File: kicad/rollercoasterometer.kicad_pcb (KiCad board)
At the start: 2 copper layers, 66 x 94 mm, 133 parts, among them J101 USB_C_Receptacle, J120 STANDOFF, J125 STANDOFF, J127 STANDOFF, J129 STANDOFF, J1401 USB_C_Receptacle, J1402 USB_C_Receptacle, J1601 USB_C_Receptacle, J1602 USB_C_Receptacle, J3501 Conn_01x10, J3502 Conn_01x10, J401 SMA, J402 SolderJumper_2_Open, Q2001 NMOS, Q3101 NMOS, Q801 NMOS, U1001 TCR2EF 1.8V, U104 Teensy4.1, U1101 BMM150, U1201 ICM-42688, U1301 ICM-42688, U1801 TLE493D-W2B6, U1901 TCR2EF 1.8V, U201 ICM-42688, U2101 ICM-42688, U2201 BMM150, U2401 AK09918, U2501 BMP384, U2701 ICM-42688, U2801 TLE493D-W2B6, U2901 BMP384, U3001 TCR2EF 1.8V, U301 USBLC6-4SC6, U3201 ICM-42688, U3301 BMM150, U3401 AK09918, U401 ZED_F9R, U501 TCR2EF 3.3V, U601 AK09918, U704 TLE493D-W2B6, U901 BMP384

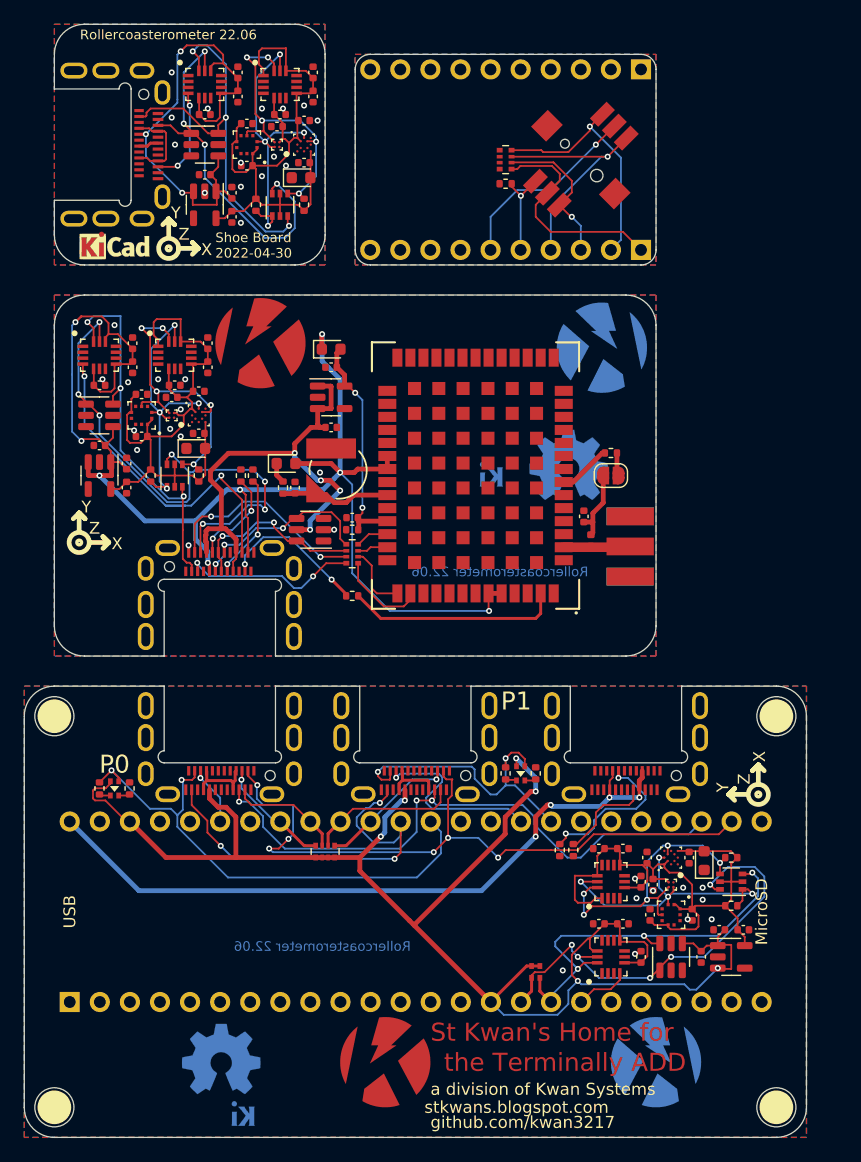
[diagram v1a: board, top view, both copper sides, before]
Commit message: Moved USB+ connectors to bottom of board
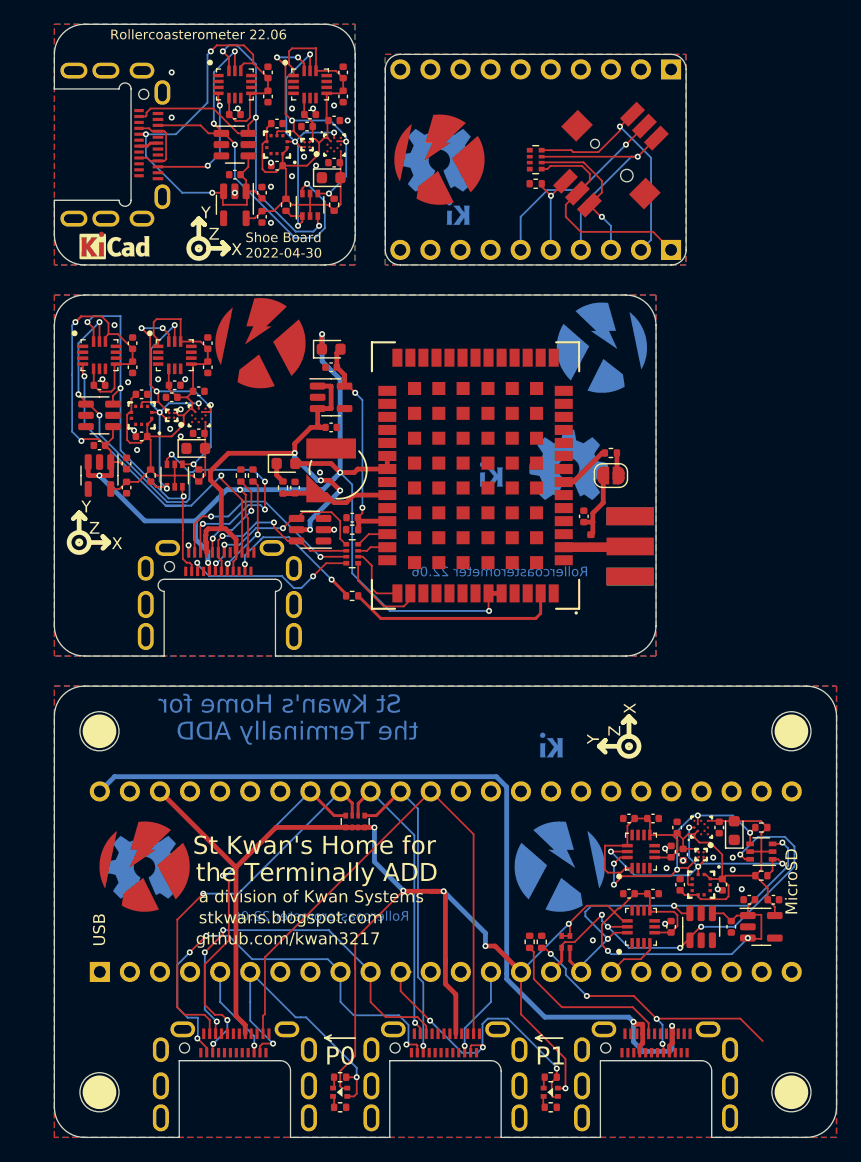
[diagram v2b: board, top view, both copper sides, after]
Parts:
- added G3502: KwanSystems, KwanSystems:StKwansSoldermask, F.Cu at (108.7, 72.4)
- added G3503: DesignedWithKicad, KwanSystems:Symbol_KiCAD-Logo_CopperAndSilkScreenTop_small, B.Cu at (108.5, 77.0)
- added G3504: OSHW, KwanSystems:OSHW-Symbol_6.7x6mm_SolderMask, B.Cu at (108.7, 72.1)
- G101: moved to F.Cu
- G102: moved to B.Cu
- moved G101 46.2 mm to (83.8, 132.1), turned to 0 degrees
- moved G103 40.6 mm to (116.3, 121.9)
- moved J101 38.2 mm to (127.0, 154.9), turned to 0 degrees
- moved J1601 38.2 mm to (109.2, 154.9), turned to 0 degrees
- moved J1401 38.1 mm to (91.4, 154.9), turned to 0 degrees
- moved R1401 32.3 mm to (100.3, 152.4), turned to 0 degrees
- moved D1401 32.0 mm to (100.3, 151.1), turned to 0 degrees
- moved R1402 31.7 mm to (100.3, 149.9), turned to 0 degrees
- moved R1601 28.2 mm to (118.1, 152.4), turned to 0 degrees
- moved D1601 27.0 mm to (118.1, 151.1), turned to 0 degrees
- moved R1602 25.9 mm to (118.1, 149.9), turned to 0 degrees
- moved G102 22.1 mm to (118.9, 132.1), turned to 180 degrees
- moved G104 17.7 mm to (83.8, 131.8)
- moved G105 11.7 mm to (124.7, 121.9)
- moved R101 8.58 mm to (116.3, 138.4), turned to -90 degrees
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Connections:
- U104 pad 10: unconnected-(U104-Pad10) -> /RX_GPS
- U104 pad 11: unconnected-(U104-Pad11) -> /P1_ID
- U104 pad 14: unconnected-(U104-Pad14) -> /P1_INT
- U104 pad 26: /TX_GPS -> unconnected-(U104-Pad26)
- U104 pad 27: /RX_GPS -> unconnected-(U104-Pad27)
- U104 pad 32: /P1_ID -> unconnected-(U104-Pad32)
- U104 pad 33: /P1_INT -> unconnected-(U104-Pad33)
- U104 pad 36: /P0_ID -> unconnected-(U104-Pad36)
- U104 pad 43: /P0_INT -> unconnected-(U104-Pad43)
- U104 pad 5: unconnected-(U104-Pad5) -> /P0_INT
- U104 pad 6: unconnected-(U104-Pad6) -> /P0_ID
- U104 pad 9: unconnected-(U104-Pad9) -> /TX_GPS
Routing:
- net /P0_SDA: track 9.50 -> 32.5 mm, vias 0 -> 1
- net /P0_SCL: track 9.80 -> 31.9 mm, vias 1 -> 3
- net /TX_GPS: track 59.0 -> 37.4 mm, vias 6 -> 4
- net +3V3: track 131.7 -> 152.8 mm, vias 6 -> 8
- net /P0_ID: track 43.6 -> 24.9 mm
- net /RX_GPS: track 50.1 -> 32.5 mm
- net +5V: track 59.6 -> 76.7 mm, vias 4 -> 2
- net /P1_SCL: track 11.7 -> 26.7 mm
- net /PPS: track 34.5 -> 48.3 mm, vias 3 -> 0
- net /CC2: track 13.3 -> 25.4 mm, vias 2 -> 4
- net /P1_SDA: track 12.7 -> 24.7 mm, vias 0 -> 1
- net /P1_INT: track 16.1 -> 7.74 mm
- net /CC1: track 8.11 -> 14.9 mm
- net unconnected-(J1401-PadA4): track 5.72 -> 0.00 mm
- net /Shoe/Q_3V3: track 41.7 -> 46.8 mm
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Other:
- outline, holes or cut-outs redrawn
- board text added: "Interface Board 2022-04-30"
- board text added: "St Kwan's Home for"
- board text added: "the Terminally ADD"

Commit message: Added a NC to the board
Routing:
- net /CC2: track 25.4 -> 15.6 mm
- net +3V3: track 152.8 -> 150.2 mm, vias 8 -> 7
- net /P1_ID: track 26.8 -> 25.9 mm
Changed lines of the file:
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@@
       (net 82 "/TV_D{slash}~{C}") (pinfunction "D5~") (pintype "bidirectional"))
     (pad "8" thru_hole oval locked (at 0 17.78 90) (size 1.7 1.7) (drill 1) (layers *.Cu *.Mask)
-      (net 239 "unconnected-(U104-Pad8)") (pinfunction "D6~") (pintype "bidirectional"))
+      (net 239 "unconnected-(U104-Pad8)") (pinfunction "D6~") (pintype "bidirectional+no_connect"))
     (pad "9" thru_hole oval locked (at 0 20.32 90) (size 1.7 1.7) (drill 1) (layers *.Cu *.Mask)
       (net 75 "/TX_GPS") (pinfunction "D7~") (pintype "bidirectional"))
@@
   (segment (start 99.3679 137.4399) (end 90.4499 137.4399) (width 0.1524) (layer "B.Cu") (net 72))
   (segment (start 134.7525 135.4755) (end 134.7525 136.21) (width 0.1524) (layer "F.Cu") (net 73))
+  (segment (start 110.095 142.861) (end 109.22 141.986) (width 0.4064) (layer "F.Cu") (net 73))
   (segment (start 101.6 140.716) (end 101.6 148.082) (width 0.1524) (layer "F.Cu") (net 73))
   (segment (start 125.194 134.366) (end 123.952 135.608) (width 0.1524) (layer "F.Cu") (net 73))
@@
   (segment (start 124.214 136.66) (end 123.444 135.89) (width 0.1524) (layer "F.Cu") (net 73))
   (segment (start 121.158 135.382) (end 119.634 136.906) (width 0.1524) (layer "F.Cu") (net 73))
-  (segment (start 109.22 134.3152) (end 109.0676 134.1628) (width 0.4064) (layer "F.Cu") (net 73))
   (segment (start 135.065742 138.176) (end 135.89 138.176) (width 0.1524) (layer "F.Cu") (net 73))
+  (segment (start 110.095 146.19) (end 110.095 142.861) (width 0.4064) (layer "F.Cu") (net 73))
   (segment (start 113.4136 138.7856) (end 115.598 140.97) (width 0.4064) (layer "F.Cu") (net 73))
   (segment (start 123.444 135.89) (end 122.936 135.382) (width 0.1524) (layer "F.Cu") (net 73))
@@
   (segment (start 123.952 135.608) (end 123.797 135.608) (width 0.1524) (layer "F.Cu") (net 73))
   (segment (start 119.3546 150.7998) (end 119.3546 148.3106) (width 0.1524) (layer "F.Cu") (net 73))
-  (segment (start 108.0008 134.1628) (end 107.1372 134.1628) (width 0.1524) (layer "F.Cu") (net 73))
   (segment (start 122.936 135.382) (end 121.158 135.382) (width 0.1524) (layer "F.Cu") (net 73))
   (segment (start 126.266 134.366) (end 125.194 134.366) (width 0.1524) (layer "F.Cu") (net 73))
@@
   (segment (start 135.354 134.874) (end 134.7525 135.4755) (width 0.1524) (layer "F.Cu") (net 73))
   (segment (start 91.532889 132.144889) (end 91.532889 144.669689) (width 0.4064) (layer "F.Cu") (net 73))
+  (segment (start 109.22 134.3152) (end 109.0676 134.1628) (width 0.4064) (layer "F.Cu") (net 73))
   (segment (start 122.428 138.684) (end 122.936 139.192) (width 0.1524) (layer "F.Cu") (net 73))
   (segment (start 134.8185 136.144) (end 134.7525 136.21) (width 0.1524) (layer "F.Cu") (net 73))
-  (segment (start 108.0008 134.1628) (end 108.5088 134.1628) (width 0.4064) (layer "F.Cu") (net 73))
-  (segment (start 105.7148 134.1628) (end 105.664 134.112) (width 0.4064) (layer "F.Cu") (net 73))
   (segment (start 119.73 137.93) (end 119.03 137.93) (width 0.1524) (layer "F.Cu") (net 73))
   (segment (start 101.6 138.176) (end 105.664 134.112) (width 0.1524) (layer "F.Cu") (net 73))
@@
   (segment (start 94.907778 128.77) (end 100.8 128.77) (width 0.4064) (layer "F.Cu") (net 73))
   (segment (start 119.73 137.002) (end 119.73 137.93) (width 0.1524) (layer "F.Cu") (net 73))
-  (segment (start 109.22 139.954) (end 109.22 140.208) (width 0.4064) (layer "F.Cu") (net 73))
   (segment (start 91.532889 132.144889) (end 94.907778 128.77) (width 0.4064) (layer "F.Cu") (net 73))
-  (segment (start 109.22 140.208) (end 109.22 134.3152) (width 0.4064) (layer "F.Cu") (net 73))
   (segment (start 134.7525 138.11) (end 134.999742 138.11) (width 0.1524) (layer "F.Cu") (net 73))
   (segment (start 128.524 135.89) (end 126.61 135.89) (width 0.1524) (layer "F.Cu") (net 73))
   (segment (start 119.634 136.906) (end 119.73 137.002) (width 0.1524) (layer "F.Cu") (net 73))
+  (segment (start 109.22 141.986) (end 109.22 134.3152) (width 0.4064) (layer "F.Cu") (net 73))
   (segment (start 122.428 137.795) (end 122.428 136.977) (width 0.1524) (layer "F.Cu") (net 73))
-  (segment (start 110.095 142.861) (end 110.095 146.19) (width 0.4064) (layer "F.Cu") (net 73))
   (segment (start 128.80812 137.10188) (end 128.80812 136.17412) (width 0.1524) (layer "F.Cu") (net 73))
-  (segment (start 109.22 140.208) (end 109.22 141.986) (width 0.4064) (layer "F.Cu") (net 73))
   (segment (start 126.48 135.76) (end 126.48 134.58) (width 0.1524) (layer "F.Cu") (net 73))
   (segment (start 102.4 128.77) (end 103.2176 128.77) (width 0.4064) (layer "F.Cu") (net 73))
   (segment (start 135.89 138.176) (end 135.89 136.144) (width 0.1524) (layer "F.Cu") (net 73))
-  (segment (start 108.5088 134.1628) (end 105.7148 134.1628) (width 0.4064) (layer "F.Cu") (net 73))
   (segment (start 126.48 134.58) (end 126.266 134.366) (width 0.1524) (layer "F.Cu") (net 73))
   (segment (start 100.33 149.352) (end 100.33 150.622) (width 0.1524) (layer "F.Cu") (net 73))
   (segment (start 103.2176 128.77) (end 103.2256 128.778) (width 0.4064) (layer "F.Cu") (net 73))
   (segment (start 132.6925 136.0225) (end 133.35 136.68) (width 0.1524) (layer "F.Cu") (net 73))
-  (segment (start 109.22 141.986) (end 110.095 142.861) (width 0.4064) (layer "F.Cu") (net 73))
   (segment (start 101.6 148.082) (end 100.33 149.352) (width 0.1524) (layer "F.Cu") (net 73))
+  (segment (start 105.7148 134.1628) (end 108.5088 134.1628) (width 0.4064) (layer "F.Cu") (net 73))
   (segment (start 123.4795 135.9255) (end 123.444 135.89) (width 0.1524) (layer "F.Cu") (net 73))
   (segment (start 128.80812 136.17412) (end 128.524 135.89) (width 0.1524) (layer "F.Cu") (net 73))
@@
   (segment (start 100.8 128.77) (end 101.35 128.77) (width 0.4064) (layer "F.Cu") (net 73))
   (segment (start 92.315 145.4518) (end 92.315 146.19) (width 0.4064) (layer "F.Cu") (net 73))
-  (segment (start 101.6 139.7) (end 101.6 140.716) (width 0.1524) (layer "F.Cu") (net 73))
+  (segment (start 105.664 134.112) (end 105.7148 134.1628) (width 0.4064) (layer "F.Cu") (net 73))
   (segment (start 101.6 140.716) (end 101.6 138.176) (width 0.1524) (layer "F.Cu") (net 73))
   (via (at 122.936 139.192) (size 0.508) (drill 0.254) (layers "F.Cu" "B.Cu") (net 73))
@@
   (via (at 119.634 136.906) (size 0.508) (drill 0.254) (layers "F.Cu" "B.Cu") (net 73))
   (via (at 109.0676 134.1628) (size 0.508) (drill 0.254) (layers "F.Cu" "B.Cu") (net 73))
-  (via (at 119.3546 150.7998) (size 0.508) (drill 0.254) (layers "F.Cu" "B.Cu") (net 73))
   (via (at 105.664 134.112) (size 0.508) (drill 0.254) (layers "F.Cu" "B.Cu") (net 73))
   (via (at 112.5982 138.7856) (size 0.508) (drill 0.254) (layers "F.Cu" "B.Cu") (net 73))
@@
   (segment (start 118.585 149.891) (end 118.196889 150.279111) (width 0.1524) (layer "F.Cu") (net 88))
   (segment (start 118.618 149.858) (end 118.585 149.891) (width 0.1524) (layer "F.Cu") (net 88))
-  (segment (start 106.3498 140.97) (end 105.438 140.97) (width 0.1524) (layer "F.Cu") (net 88))
   (segment (start 118.196889 151.435289) (end 118.2726 151.511) (width 0.1524) (layer "F.Cu") (net 88))
   (segment (start 111.345 147.2376) (end 111.420711 147.161889) (width 0.1524) (layer "F.Cu") (net 88))
@@
   (segment (start 119.0559 143.9479) (end 125.0381 143.9479) (width 0.1524) (layer "F.Cu") (net 208))
   (segment (start 116.676111 139.284111) (end 116.676111 141.568111) (width 0.1524) (layer "F.Cu") (net 208))
-  (segment (start 127.07132 144.91188) (end 134.11888 144.91188) (width 0.1524) (layer "F.Cu") (net 209))
   (segment (start 125.1204 143.002) (end 127.0508 144.9324) (width 0.1524) (layer "F.Cu") (net 209))
   (segment (start 127.625 147.122676) (end 127.546574 147.04425) (width 0.1524) (layer "F.Cu") (net 209))
   (segment (start 127.625 147.79) (end 127.625 147.122676) (width 0.1524) (layer "F.Cu") (net 209))
-  (segment (start 127.0508 144.9324) (end 127.07132 144.91188) (width 0.1524) (layer "F.Cu") (net 209))
   (segment (start 117.604 138.94) (end 118.11 139.446) (width 0.1524) (layer "F.Cu") (net 209))
-  (segment (start 134.11888 144.91188) (end 136.017 146.81) (width 0.1524) (layer "F.Cu") (net 209))
   (segment (start 117.348 138.94) (end 117.604 138.94) (width 0.1524) (layer "F.Cu") (net 209))
   (segment (start 121.158 143.002) (end 125.1204 143.002) (width 0.1524) (layer "F.Cu") (net 209))

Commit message: Checkin before branch
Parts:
- J402: value SolderJumper_2_Open -> NormallyClosed; footprint Jumper:SolderJumper-2_P1.3mm_Open_RoundedPad1.0x1.5mm -> KwanSystems:SolderJumper-2_P1.3mm_MaskBridged_RoundedPad1.0x1.5mm
- S3501: value JS1400 -> JS5208; footprint KwanSystems:JS1400 -> KwanSystems:JS5208
- moved S3501 2.54 mm to (120.7, 72.4), turned to 0 degrees
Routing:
- net /Shoulder/GPS Rover/V_RF: track 4.49 -> 5.31 mm
